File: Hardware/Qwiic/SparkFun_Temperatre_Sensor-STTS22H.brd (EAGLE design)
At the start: 25.4 x 25.4 mm, 54 parts, among them J1 QWIIC_RIGHT_ANGLE, J2 QWIIC_RIGHT_ANGLE, U2 STTS22H

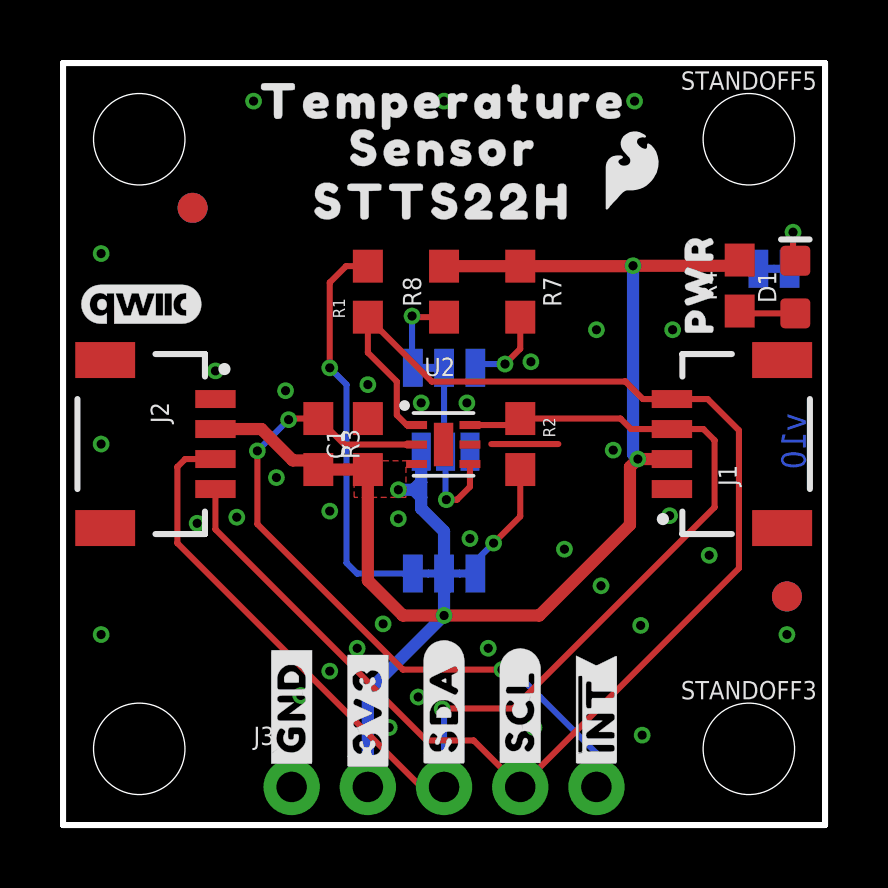
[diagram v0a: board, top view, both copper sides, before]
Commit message: Adds Qwiic Micro shell of a design
* Adds folders for hardware files
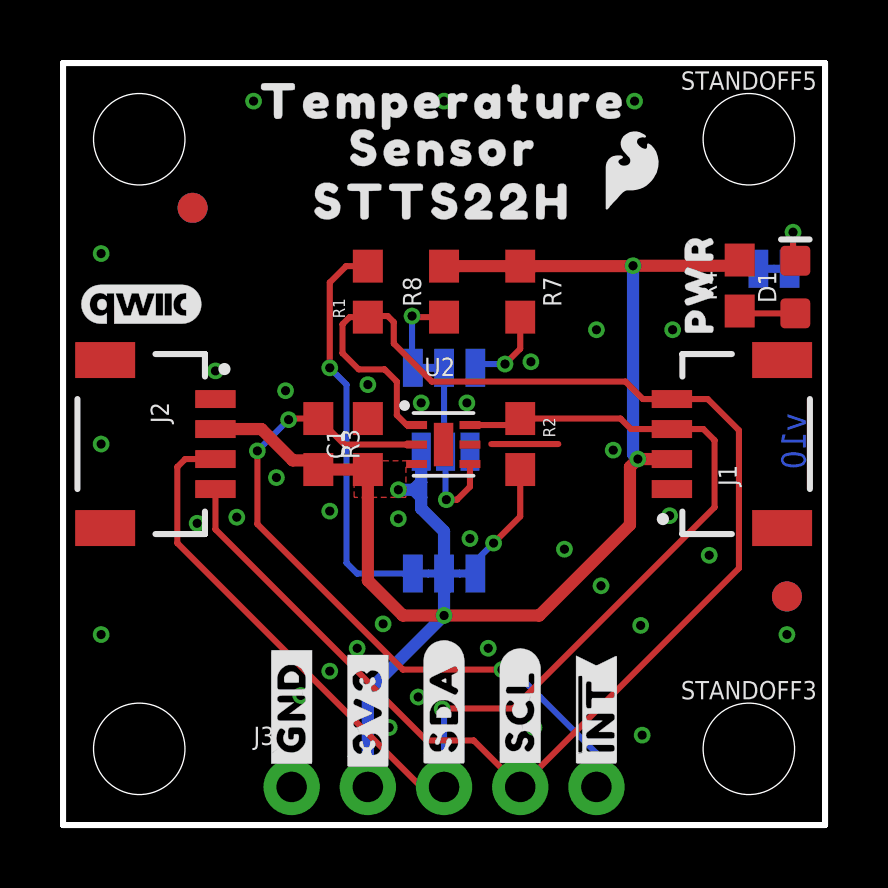
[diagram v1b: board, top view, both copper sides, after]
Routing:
- net SCL: track 48.4 -> 50.4 mm
- net N$4: track 3.34 -> 2.82 mm
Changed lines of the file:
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@@
 <layer number="19" name="Unrouted" color="6" fill="1" visible="yes" active="yes"/>
 <layer number="20" name="Dimension" color="15" fill="1" visible="yes" active="yes"/>
-<layer number="21" name="tPlace" color="16" fill="1" visible="no" active="yes"/>
-<layer number="22" name="bPlace" color="14" fill="1" visible="no" active="yes"/>
+<layer number="21" name="tPlace" color="16" fill="1" visible="yes" active="yes"/>
+<layer number="22" name="bPlace" color="14" fill="1" visible="yes" active="yes"/>
 <layer number="23" name="tOrigins" color="15" fill="1" visible="yes" active="yes"/>
 <layer number="24" name="bOrigins" color="15" fill="1" visible="yes" active="yes"/>
@@
 <layer number="37" name="tTest" color="7" fill="1" visible="no" active="yes"/>
 <layer number="38" name="bTest" color="7" fill="1" visible="no" active="yes"/>
-<layer number="39" name="tKeepout" color="4" fill="11" visible="yes" active="yes"/>
+<layer number="39" name="tKeepout" color="4" fill="11" visible="no" active="yes"/>
 <layer number="40" name="bKeepout" color="1" fill="11" visible="no" active="yes"/>
 <layer number="41" name="tRestrict" color="4" fill="10" visible="no" active="yes"/>
@@
 <contactref element="R7" pad="1"/>
 <contactref element="ADDR1" pad="3"/>
-<wire x1="8.509" y1="11.85" x2="8.47" y2="11.811" width="0.4064" layer="1"/>
 <wire x1="5.08" y1="13.2" x2="6.612" y2="13.2" width="0.4064" layer="1"/>
 <wire x1="11.3284" y1="6.985" x2="12.7" y2="6.985" width="0.4064" layer="1"/>
@@
 <contactref element="R1" pad="2"/>
 <contactref element="I2C_PU" pad="1"/>
-<wire x1="11.6586" y1="8.7884" x2="11.6586" y2="8.382" width="0.2032" layer="16"/>
 <wire x1="9.4488" y1="8.7376" x2="9.4488" y2="14.6812" width="0.2032" layer="16"/>
 <wire x1="9.4488" y1="14.6812" x2="8.89" y2="15.24" width="0.2032" layer="16"/>
@@
 <contactref element="ADDR" pad="3"/>
 <contactref element="R8" pad="1"/>
-<wire x1="12.7" y1="16.93" x2="12.358" y2="16.93" width="0.2032" layer="1"/>
-<wire x1="11.5316" y1="15.367" x2="11.6586" y2="15.24" width="0.2032" layer="16"/>
 <wire x1="12.7" y1="16.93" x2="11.6704" y2="16.93" width="0.2032" layer="1"/>
 <wire x1="11.6704" y1="16.93" x2="11.6332" y2="16.9672" width="0.2032" layer="1"/>
@@
 <contactref element="J2" pad="4"/>
 <contactref element="J3" pad="4"/>
-<wire x1="20.2946" y1="14.2" x2="19.328" y2="14.2" width="0.2032" layer="1"/>
+<wire x1="19.328" y1="14.2" x2="20.2946" y2="14.2" width="0.2032" layer="1"/>
 <wire x1="20.2946" y1="14.2" x2="21.487" y2="14.2" width="0.2032" layer="1"/>
 <wire x1="21.487" y1="14.2" x2="22.5298" y2="13.1572" width="0.2032" layer="1"/>
@@
 <wire x1="15.24" y1="1.27" x2="22.5298" y2="8.5598" width="0.2032" layer="1"/>
 <wire x1="5.08" y1="9.8552" x2="5.08" y2="11.2" width="0.2032" layer="1"/>
-<wire x1="19.328" y1="14.2" x2="18.7452" y2="14.7828" width="0.2032" layer="1"/>
-<wire x1="18.7452" y1="14.7828" x2="18.7325" y2="14.7955" width="0.2032" layer="1"/>
 <wire x1="12.1158" y1="2.8194" x2="5.08" y2="9.8552" width="0.2032" layer="1"/>
 <wire x1="15.24" y1="1.27" x2="13.6906" y2="2.8194" width="0.2032" layer="1"/>
@@
 <wire x1="11.784" y1="13.334" x2="11.4564" y2="13.334" width="0.2032" layer="1"/>
 <wire x1="11.4564" y1="13.334" x2="11.1252" y2="13.6652" width="0.2032" layer="1"/>
-<wire x1="10.16" y1="15.748" x2="10.16" y2="16.93" width="0.2032" layer="1"/>
+<wire x1="10.16" y1="16.93" x2="9.5504" y2="16.93" width="0.2032" layer="1"/>
+<wire x1="9.315" y1="16.6946" x2="9.5504" y2="16.93" width="0.2032" layer="1"/>
 <wire x1="11.1252" y1="13.6652" x2="11.1252" y2="14.7828" width="0.2032" layer="1"/>
-<wire x1="11.1252" y1="14.7828" x2="10.16" y2="15.748" width="0.2032" layer="1"/>
+<wire x1="11.1252" y1="14.7828" x2="10.7188" y2="15.1892" width="0.2032" layer="1"/>
 <wire x1="12.2936" y1="14.7828" x2="18.7452" y2="14.7828" width="0.2032" layer="1"/>
-<wire x1="12.2936" y1="14.7828" x2="10.16" y2="16.9164" width="0.2032" layer="1"/>
-<wire x1="10.16" y1="16.93" x2="10.16" y2="16.9164" width="0.2032" layer="1"/>
+<wire x1="18.7452" y1="14.7828" x2="19.328" y2="14.2" width="0.2032" layer="1"/>
+<wire x1="10.7188" y1="15.1892" x2="9.8552" y2="15.1892" width="0.2032" layer="1"/>
+<wire x1="9.315" y1="15.7294" x2="9.315" y2="16.6946" width="0.2032" layer="1"/>
+<wire x1="9.8552" y1="15.1892" x2="9.315" y2="15.7294" width="0.2032" layer="1"/>
+<wire x1="10.16" y1="16.93" x2="10.1972" y2="16.9672" width="0.2032" layer="1"/>
+<wire x1="10.1972" y1="16.9672" x2="10.8204" y2="16.9672" width="0.2032" layer="1"/>
+<wire x1="10.8204" y1="16.9672" x2="11.0236" y2="16.764" width="0.2032" layer="1"/>
+<wire x1="11.0236" y1="16.764" x2="11.0236" y2="16.0528" width="0.2032" layer="1"/>
+<wire x1="11.0236" y1="16.0528" x2="12.2936" y2="14.7828" width="0.2032" layer="1"/>
 </signal>
 <signal name="SDA">
@@
 <contactref element="J2" pad="3"/>
 <contactref element="J3" pad="3"/>
-<wire x1="13.564" y1="13.334" x2="13.565" y2="13.335" width="0.2032" layer="1"/>
 <wire x1="21.717" y1="12.827" x2="21.717" y2="10.5918" width="0.2032" layer="1"/>
 <wire x1="21.717" y1="10.5918" x2="15.0114" y2="3.8862" width="0.2032" layer="1"/>

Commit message: Adds note for default addresses
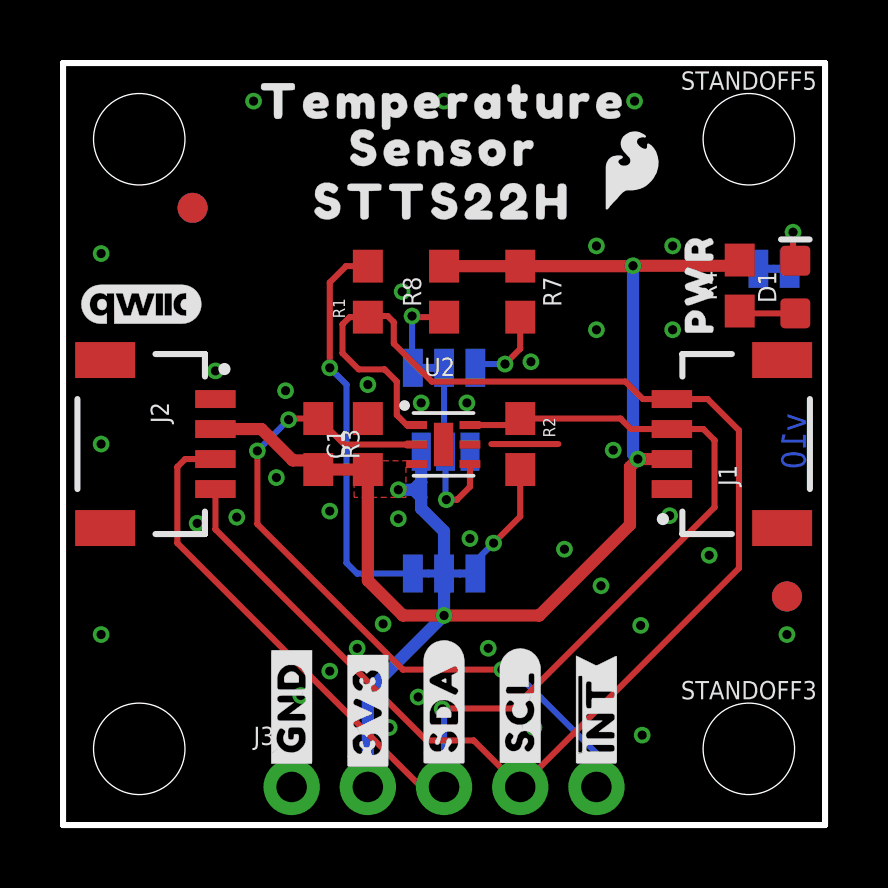
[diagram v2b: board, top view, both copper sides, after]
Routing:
- net GND: vias 37 -> 40
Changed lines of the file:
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@@
 <setting verticaltext="up"/>
 </settings>
-<grid distance="0.05" unitdist="inch" unit="inch" style="dots" multiple="1" display="yes" altdistance="0.002" altunitdist="inch" altunit="inch"/>
+<grid distance="0.05" unitdist="inch" unit="inch" style="dots" multiple="1" display="yes" altdistance="0.005" altunitdist="inch" altunit="inch"/>
 <layers>
 <layer number="1" name="Top" color="4" fill="1" visible="yes" active="yes"/>
@@
 <via x="17.78" y="16.51" extent="1-16" drill="0.3048"/>
 <contactref element="C1" pad="2"/>
+<via x="11.303" y="17.78" extent="1-16" drill="0.3048"/>
+<via x="17.78" y="19.304" extent="1-16" drill="0.3048"/>
+<via x="20.32" y="19.304" extent="1-16" drill="0.3048"/>
 </signal>
 <signal name="3.3V">

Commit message: Fixes off center footprint, adds center pad on temp sensor to ground
*
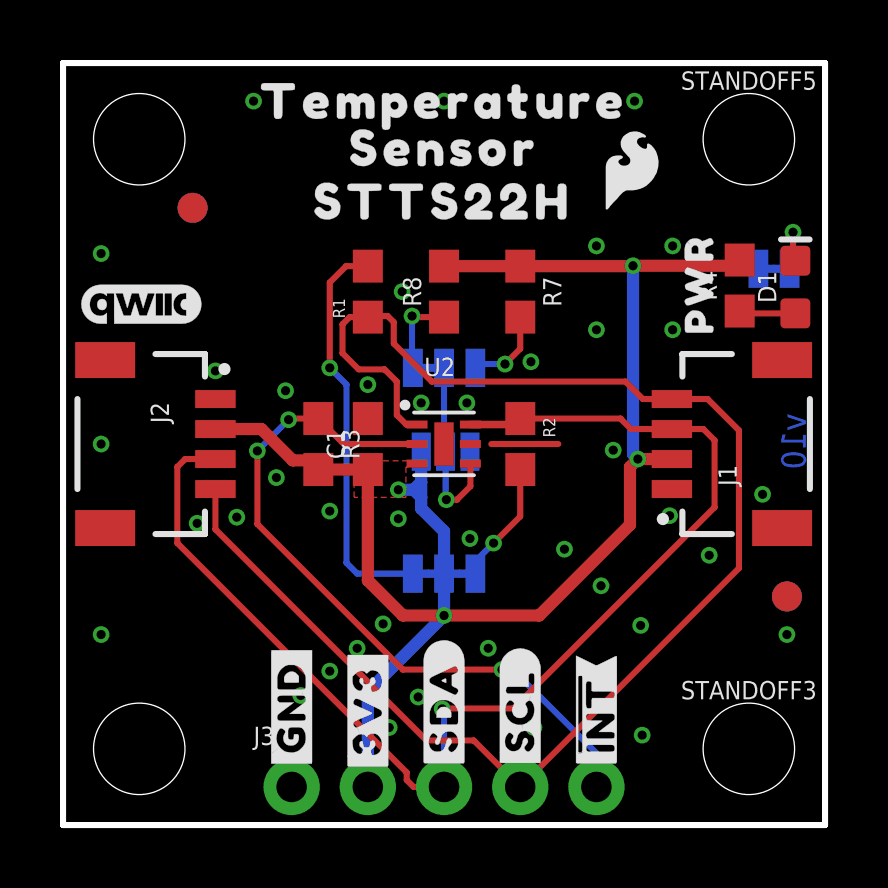
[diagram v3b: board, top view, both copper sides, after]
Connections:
- net GND: now also U2.P7
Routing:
- net GND: vias 40 -> 41
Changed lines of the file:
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@@
 <via x="17.78" y="19.304" extent="1-16" drill="0.3048"/>
 <via x="20.32" y="19.304" extent="1-16" drill="0.3048"/>
+<contactref element="U2" pad="P7"/>
+<via x="23.3172" y="11.0236" extent="1-16" drill="0.3048"/>
 </signal>
 <signal name="3.3V">
@@
 <contactref element="U2" pad="P2"/>
 <contactref element="R3" pad="1"/>
-<wire x1="11.784" y1="12.684" x2="11.43" y2="12.684" width="0.2032" layer="1"/>
-<wire x1="11.43" y1="12.684" x2="9.375" y2="12.684" width="0.2032" layer="1"/>
-<wire x1="9.375" y1="12.684" x2="8.509" y2="13.55" width="0.2032" layer="1"/>
+<wire x1="9.375" y1="12.684" x2="9.359" y2="12.7" width="0.2032" layer="1"/>
+<wire x1="9.315" y1="12.744" x2="8.509" y2="13.55" width="0.2032" layer="1"/>
 <wire x1="8.509" y1="13.55" x2="7.5556" y2="13.55" width="0.2032" layer="1"/>
 <wire x1="7.5184" y1="13.5128" x2="7.5556" y2="13.55" width="0.2032" layer="1"/>
@@
 <wire x1="14.986" y1="5.1816" x2="14.6304" y2="5.1816" width="0.2032" layer="16"/>
 <wire x1="15.9004" y1="4.2672" x2="14.986" y2="5.1816" width="0.2032" layer="16"/>
+<wire x1="11.799" y1="12.7" x2="9.359" y2="12.7" width="0.2032" layer="1"/>
+<wire x1="9.359" y1="12.7" x2="9.315" y2="12.744" width="0.2032" layer="1"/>
 </signal>
 <signal name="N$4">
@@
 <wire x1="12.7508" y1="10.8712" x2="12.7762" y2="10.8458" width="0.2032" layer="16"/>
 <via x="12.7762" y="10.8458" extent="1-16" drill="0.3048"/>
-<wire x1="13.564" y1="12.034" x2="13.564" y2="11.2776" width="0.2032" layer="1"/>
-<wire x1="12.7762" y1="10.8458" x2="13.1322" y2="10.8458" width="0.2032" layer="1"/>
-<wire x1="13.1322" y1="10.8458" x2="13.564" y2="11.2776" width="0.2032" layer="1"/>
+<wire x1="13.1322" y1="10.8458" x2="12.7762" y2="10.8458" width="0.2032" layer="1"/>
+<wire x1="13.579" y1="12.05" x2="13.579" y2="11.2926" width="0.2032" layer="1"/>
+<wire x1="13.579" y1="11.2926" x2="13.1322" y2="10.8458" width="0.2032" layer="1"/>
 </signal>
 <signal name="SCL">
@@
 <wire x1="15.24" y1="1.27" x2="13.6906" y2="2.8194" width="0.2032" layer="1"/>
 <wire x1="13.6906" y1="2.8194" x2="12.1158" y2="2.8194" width="0.2032" layer="1"/>
-<wire x1="11.784" y1="13.334" x2="11.4564" y2="13.334" width="0.2032" layer="1"/>
-<wire x1="11.4564" y1="13.334" x2="11.1252" y2="13.6652" width="0.2032" layer="1"/>
 <wire x1="10.16" y1="16.93" x2="9.5504" y2="16.93" width="0.2032" layer="1"/>
 <wire x1="9.315" y1="16.6946" x2="9.5504" y2="16.93" width="0.2032" layer="1"/>
@@
 <wire x1="11.0236" y1="16.764" x2="11.0236" y2="16.0528" width="0.2032" layer="1"/>
 <wire x1="11.0236" y1="16.0528" x2="12.2936" y2="14.7828" width="0.2032" layer="1"/>
+<wire x1="11.799" y1="13.35" x2="11.4404" y2="13.35" width="0.2032" layer="1"/>
+<wire x1="11.4404" y1="13.35" x2="11.1252" y2="13.6652" width="0.2032" layer="1"/>
 </signal>
 <signal name="SDA">
@@
 <wire x1="18.931" y1="13.2" x2="20.2946" y2="13.2" width="0.2032" layer="1"/>
 <wire x1="18.581" y1="13.55" x2="18.931" y2="13.2" width="0.2032" layer="1"/>
-<wire x1="13.564" y1="13.334" x2="15.239" y2="13.334" width="0.2032" layer="1"/>
 <wire x1="15.455" y1="13.55" x2="15.24" y2="13.55" width="0.2032" layer="1"/>
 <wire x1="15.239" y1="13.334" x2="15.455" y2="13.55" width="0.2032" layer="1"/>
 <wire x1="20.2946" y1="13.2" x2="21.344" y2="13.2" width="0.2032" layer="1"/>
 <wire x1="21.344" y1="13.2" x2="21.717" y2="12.827" width="0.2032" layer="1"/>
-<wire x1="12.7" y1="1.27" x2="11.938" y2="1.27" width="0.2032" layer="1"/>
-<wire x1="11.938" y1="1.27" x2="3.81" y2="9.398" width="0.2032" layer="1"/>
 <wire x1="3.81" y1="9.398" x2="3.81" y2="11.938" width="0.2032" layer="1"/>
+<wire x1="13.579" y1="13.35" x2="15.223" y2="13.35" width="0.254" layer="1"/>
+<wire x1="15.223" y1="13.35" x2="15.239" y2="13.334" width="0.254" layer="1"/>
+<wire x1="12.7" y1="1.27" x2="11.684" y2="1.27" width="0.2032" layer="1"/>
+<wire x1="11.684" y1="1.27" x2="11.4554" y2="1.4986" width="0.2032" layer="1"/>
+<wire x1="11.4554" y1="1.4986" x2="11.4554" y2="1.7526" width="0.2032" layer="1"/>
+<wire x1="11.4554" y1="1.7526" x2="3.81" y2="9.398" width="0.2032" layer="1"/>
 </signal>
 </signals>
